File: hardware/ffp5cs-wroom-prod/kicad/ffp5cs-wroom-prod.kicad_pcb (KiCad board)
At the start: 2 copper layers, 150 x 100 mm, 73 parts, among them J1 Bornier_5.08, J10 JST-XH, J11 Bornier_5.08, J12 Bornier_5.08, J13 Support OLED, J14 Support I2C ext, J15 Header servo, J16 Header servo, J17 Header GPIO libres, J18 Support I2C libre, J19 Support I2C libre, J2 Jack 5.5/2.1, J3 Bornier_5.08, J4 Bornier_5.08, J5 Bornier_5.08, J6 Bornier_5.08, J7 JST-XH, J8 JST-XH, J9 JST-XH, K1 SRD-05VDC-SL-C, K2 SRD-05VDC-SL-C, K3 SRD-05VDC-SL-C, K4 SRD-05VDC-SL-C, Q1 BC337-40, Q2 BC337-40, Q3 BC337-40, Q4 BC337-40

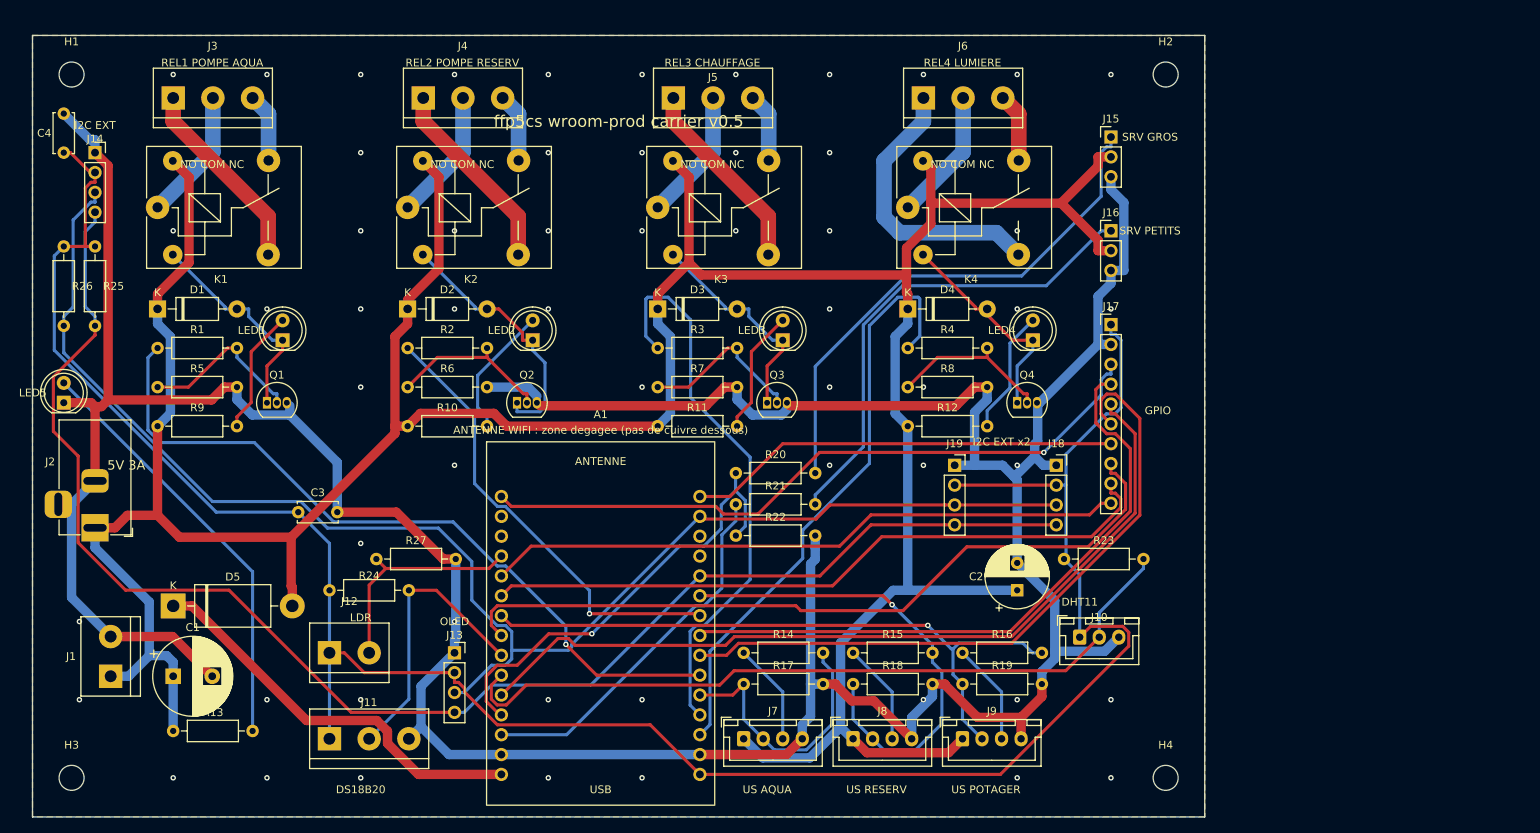
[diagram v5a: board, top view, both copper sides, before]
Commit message: feat(hardware+ffp5cs): carte 12/24V bi-module — site A2 ESP32-S3-DevKitC-1 (rev 0.6, firmware v15.27)
Option A : la carte porteuse ffp5cs-wroom-prod accueille au choix un DevKit V1
WROOM (site A1, 2x15) ou un ESP32-S3-DevKitC-1 (site A2, 2x22) — un seul module
peuplé. Chaque net fonctionnel touche les deux sites ; carte agrandie 150x100 ->
190x100 mm, header J20 = breakout GPIO S3 (AUX1=IO47, AUX2=IO42).

Firmware v15.27 : nouvelle cartographie Pins « carrier » sélectionnée par
-DPINMAP_S3_CARRIER (env wroom-s3-carrier-test, ajouté à la CI). La cartographie
S3 historique (système câblé main en production) est INCHANGÉE. Corrections
intégrées au carrier : ONE_WIRE 37->41 (PSRAM octale), ULTRASON_POTA 45->5 et
LUMINOSITE 3->1 (strapping), AUX2 48->42 (LED RGB du DevKitC-1).

Pipeline : generate.py (symbole+empreinte S3 44p, keepout antenne A2),
route_lv.py (SEED_TRACKS pads pincés/rives encombrées + VIA_BLOCKS anti-court
freerouting), tidy_silkscreen, export_fab. Validations : ERC 0, DRC 0/0/0,
garde anti-dérive 16+16 signaux (2 sites, broches S3 interdites vérifiées),
zip fab 10 fichiers (PTH 367 + NPTH 4), builds wroom-test / wroom-s3-test /
wroom-s3-carrier-test SUCCESS.

Co-Authored-By: Claude <noreply@anthropic.com>
Claude-Session: https://claude.ai/code/session_01HcxShQb65yktRwp31wBq9q
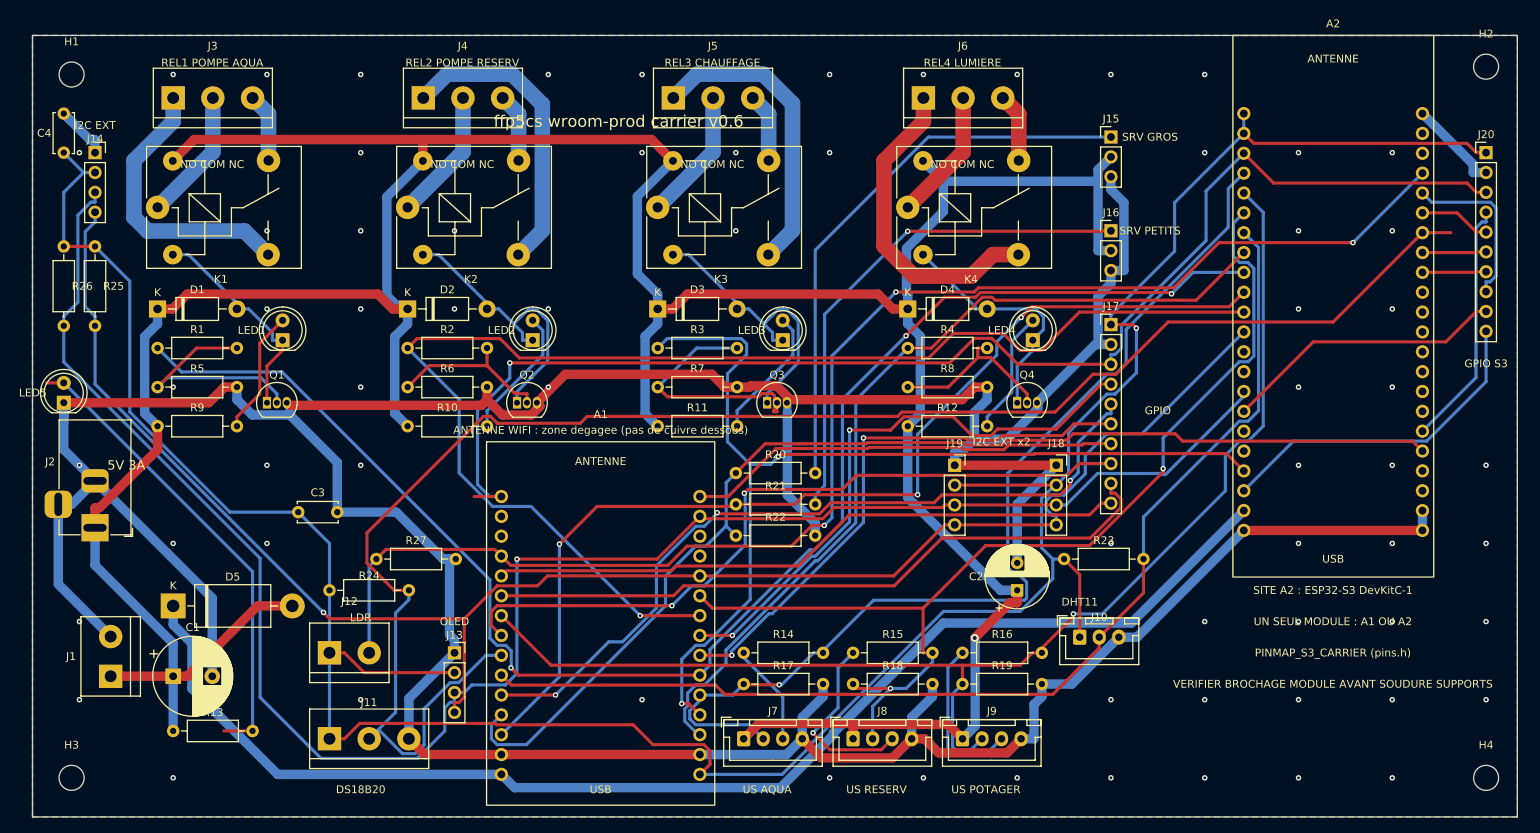
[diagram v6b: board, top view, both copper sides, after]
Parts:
- added A2: ESP32-S3-DevKitC-1, ffp5cs:ESP32_S3_DevKitC_1_44pin, F.Cu at (195.0, 55.0)
- added J20: Header GPIO S3, ffp5cs:PinHeader_1x10_P2.54mm_Vertical, F.Cu at (226.0, 60.0)
- moved H2 41.0 mm to (226.0, 49.0)
- moved H4 41.0 mm to (226.0, 140.0)
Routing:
- net ONEWIRE_GPIO26: track 36.4 -> 212.1 mm
- net LDR_GPIO34: track 28.8 -> 180.5 mm, vias 0 -> 3
- net VIN_5V: track 51.8 -> 166.3 mm
- net PUMP_TANK_GPIO18: track 58.5 -> 169.8 mm
- net PUMP_AQUA_GPIO16: track 96.0 -> 193.9 mm, vias 1 -> 3
- net US_AQUA_GPIO4: track 34.6 -> 130.1 mm, vias 0 -> 1
- net SERVO_GROS_GPIO12: track 58.4 -> 147.9 mm, vias 1 -> 0
- net SERVO_PETITS_GPIO13: track 47.4 -> 133.9 mm, vias 0 -> 3
- net EN: track 88.8 -> 171.5 mm
- net US_POTA_GPIO33: track 84.8 -> 162.6 mm
- net US_TANK_GPIO19: track 61.9 -> 135.3 mm, vias 1 -> 2
- net +3V3: track 288.9 -> 360.5 mm, vias 0 -> 1
- net GND: track 483.7 -> 552.0 mm, vias 57 -> 68
- net HEATER_GPIO2: track 71.9 -> 132.3 mm, vias 0 -> 2
- net I2C_SCL_GPIO22: track 187.9 -> 237.3 mm, vias 0 -> 1
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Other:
- board size 150 x 100 mm -> 190 x 100 mm
- board text added: "GPIO S3"
- board text added: "PINMAP_S3_CARRIER (pins.h)"
- board text added: "SITE A2 : ESP32-S3 DevKitC-1"
- board text added: "UN SEUL MODULE : A1 OU A2"
- board text added: "VERIFIER BROCHAGE MODULE AVANT SOUDURE SUPPORTS"
- board text added: "ffp5cs wroom-prod carrier v0.6"
- board text removed: "ffp5cs wroom-prod carrier v0.5"
